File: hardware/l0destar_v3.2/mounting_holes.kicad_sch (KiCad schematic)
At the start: 4 parts

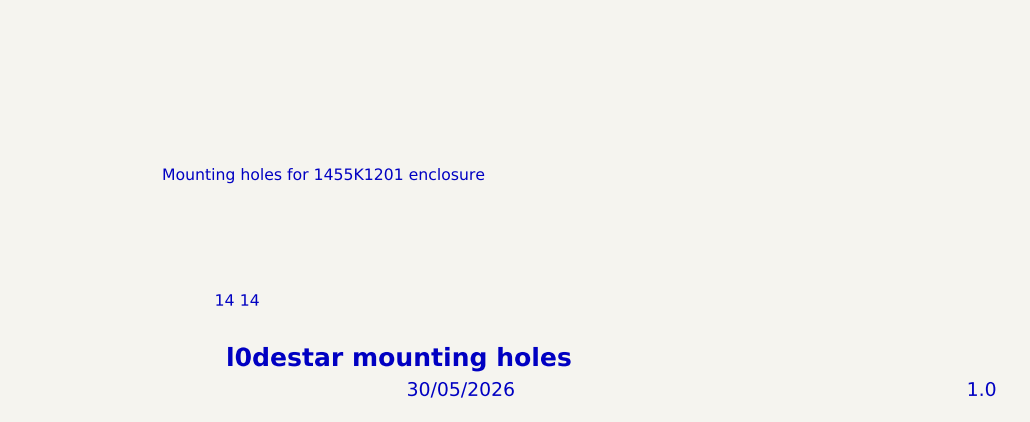
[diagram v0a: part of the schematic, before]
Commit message: update sheet annotations
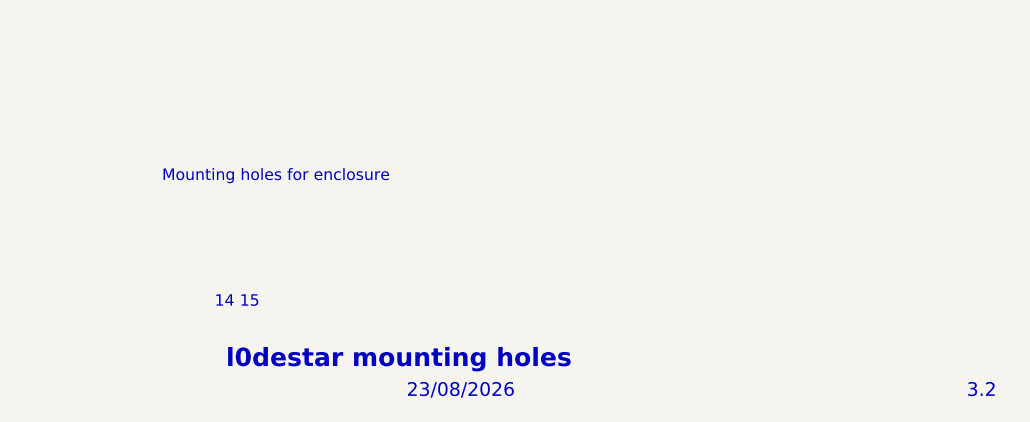
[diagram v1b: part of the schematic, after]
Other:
- note added: "15"
- note added: "23/08/2026"
- note added: "3.2"
- note added: "Mounting holes for enclosure"
- note removed: "1.0"
- note removed: "30/05/2026"
- note removed: "Mounting holes for 1455K1201 enclosure"
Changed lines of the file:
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@@
 		)
 	)
-	(text "Mounting holes for 1455K1201 enclosure"
+	(text "Mounting holes for enclosure"
 		(exclude_from_sim no)
 		(at 179.07 169.418 0)
@@
 		)
 	)
-	(text "14"
+	(text "15"
 		(exclude_from_sim no)
 		(at 187.706 183.388 0)
@@
 		)
 	)
-	(text "1.0"
+	(text "3.2"
 		(exclude_from_sim no)
 		(at 268.478 193.294 0)
@@
 		)
 	)
-	(text "30/05/2026"
+	(text "23/08/2026"
 		(exclude_from_sim no)
 		(at 206.248 193.294 0)
